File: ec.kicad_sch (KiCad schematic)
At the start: 50 parts, among them IC1 ADM3260ARSZ-RL7, J1 EC, J2 Temp, U2 ADS1115IDGS, U4 TPS60400DBV, U5 LM324, U6 MCP4017T-502E/LT

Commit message: Update files to KiCad 10.0
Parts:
- U2: footprint Package_SO:VSSOP-10_3x3mm_P0.5mm -> Package_SO:TSSOP-10_3x3mm_P0.5mm

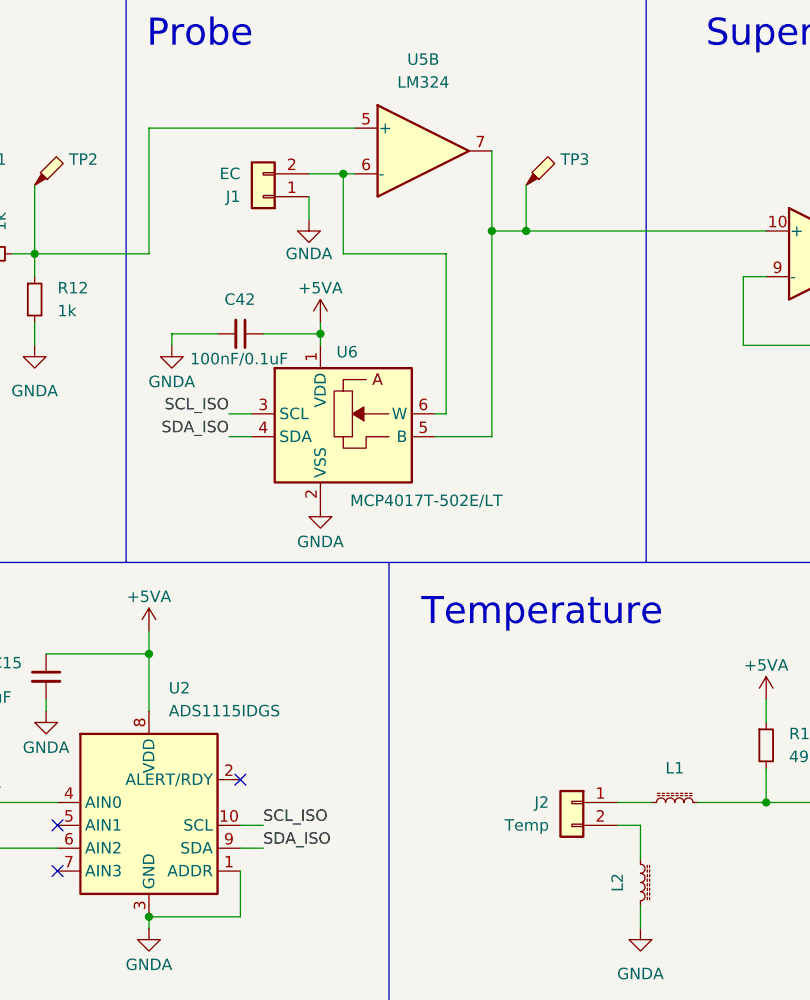
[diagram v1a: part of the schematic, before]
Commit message: Update fabrication properties
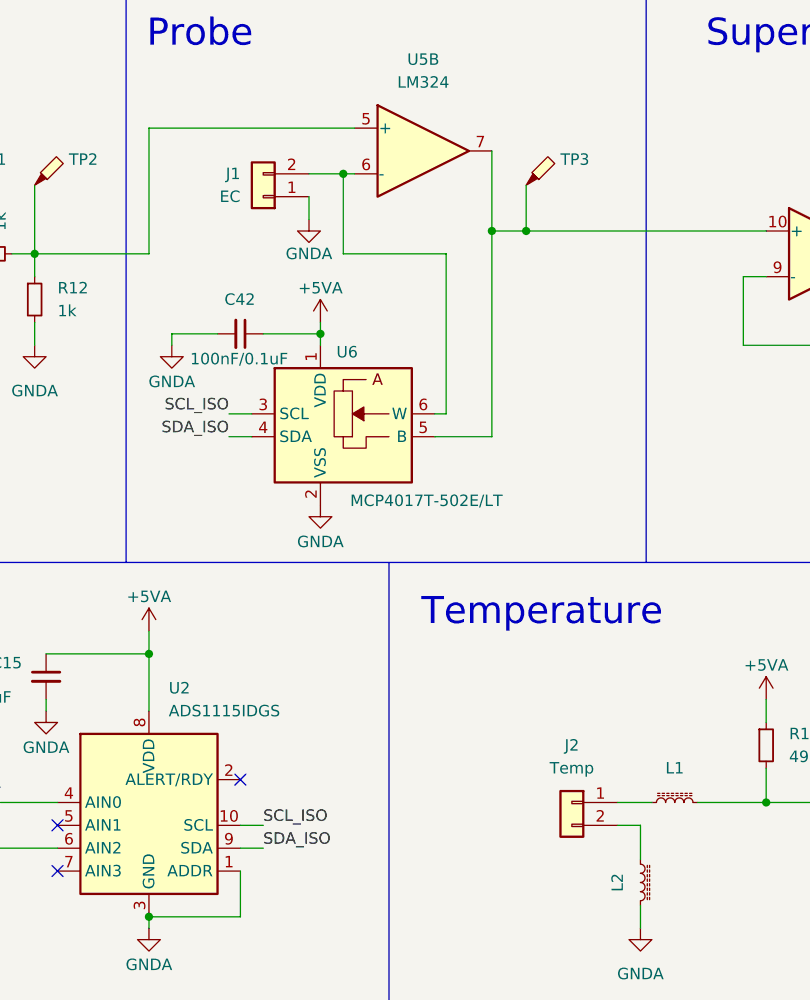
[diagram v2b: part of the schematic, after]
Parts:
- J1: value EC -> S2B-XH-A(LF)(SN)
- J2: value Temp -> S2B-XH-A(LF)(SN)
- R1: LCSC C23022 -> C2930090
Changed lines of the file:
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@@
 		(in_bom no)
 		(on_board yes)
-		(in_pos_files yes)
+		(in_pos_files no)
 		(dnp no)
 		(fields_autoplaced yes)
@@
 		(in_bom no)
 		(on_board yes)
-		(in_pos_files yes)
+		(in_pos_files no)
 		(dnp no)
 		(fields_autoplaced yes)
@@
 		(in_bom no)
 		(on_board yes)
-		(in_pos_files yes)
+		(in_pos_files no)
 		(dnp no)
 		(property "Reference" "TP5"
@@
 		(in_pos_files yes)
 		(dnp no)
+		(fields_autoplaced yes)
 		(property "Reference" "J1"
-			(at 161.29 35.5601 0)
+			(at 161.29 33.0199 0)
 			(show_name no)
 			(do_not_autoplace no)
@@
 			)
 		)
-		(property "Value" "EC"
+		(property "Value" "S2B-XH-A(LF)(SN)"
 			(at 161.29 33.0201 0)
+			(hide yes)
 			(show_name no)
 			(do_not_autoplace no)
@@
 			)
 		)
-		(property "Description" "Generic connector, single row, 01x02, script generated (kicad-library-utils/schlib/autogen/connector/)"
-			(at 163.83 35.56 0)
-			(hide yes)
+		(property "Description" "EC"
+			(at 161.29 35.5599 0)
 			(show_name no)
 			(do_not_autoplace no)
@@
 					(size 1.27 1.27)
 				)
+				(justify left)
 			)
 		)
@@
 			)
 		)
-		(property "LCSC alt" ""
-			(at 163.83 35.56 0)
-			(hide yes)
-			(show_name no)
-			(do_not_autoplace no)
-			(effects
-				(font
-					(size 1.27 1.27)
-				)
-			)
-		)
 		(property "JLCPCB Position Offset" "0,3.5"
 			(at 163.83 35.56 0)
@@
 		(in_bom no)
 		(on_board yes)
-		(in_pos_files yes)
+		(in_pos_files no)
 		(dnp no)
 		(fields_autoplaced yes)
@@
 		(in_bom no)
 		(on_board yes)
-		(in_pos_files yes)
+		(in_pos_files no)
 		(dnp no)
 		(fields_autoplaced yes)
@@
 			)
 		)
-		(property "LCSC" "C23022"
-			(at 90.17 120.65 0)
-			(hide yes)
-			(show_name no)
-			(do_not_autoplace no)
-			(effects
-				(font
-					(size 1.27 1.27)
-				)
-			)
-		)
-		(property "LCSC alt" ""
+		(property "LCSC" "C2930090"
 			(at 90.17 120.65 0)
 			(hide yes)
@@
 		(in_pos_files yes)
 		(dnp no)
+		(fields_autoplaced yes)
 		(property "Reference" "J2"
-			(at 195.58 102.8699 0)
+			(at 198.12 96.52 0)
 			(show_name no)
 			(do_not_autoplace no)
@@
 					(size 1.27 1.27)
 				)
-				(justify left)
 			)
 		)
-		(property "Value" "Temp"
+		(property "Value" "S2B-XH-A(LF)(SN)"
 			(at 195.58 105.4099 0)
+			(hide yes)
 			(show_name no)
 			(do_not_autoplace no)
@@
 			)
 		)
-		(property "Description" "Generic connector, single row, 01x02, script generated (kicad-library-utils/schlib/autogen/connector/)"
-			(at 198.12 102.87 0)
-			(hide yes)
+		(property "Description" "Temp"
+			(at 198.12 99.06 0)
 			(show_name no)
 			(do_not_autoplace no)

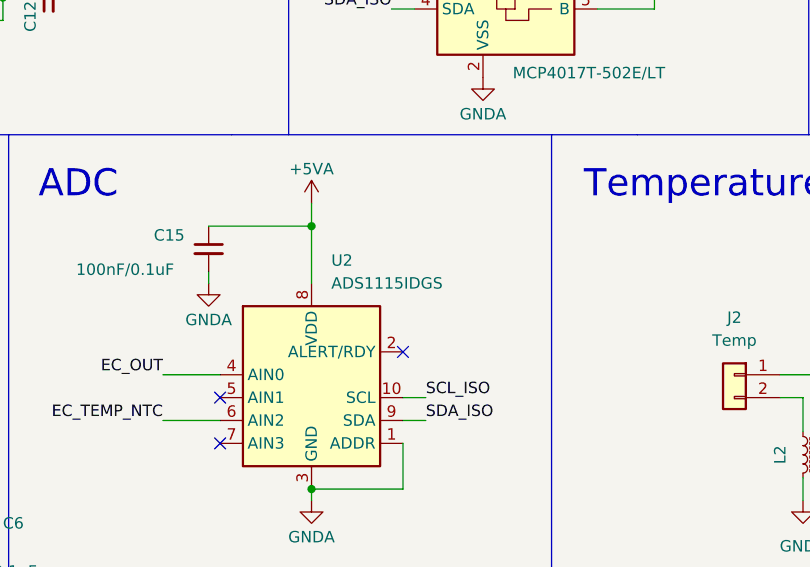
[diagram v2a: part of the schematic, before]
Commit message: Change package if ADS1115 ADC Smaller, in stock and cheaper
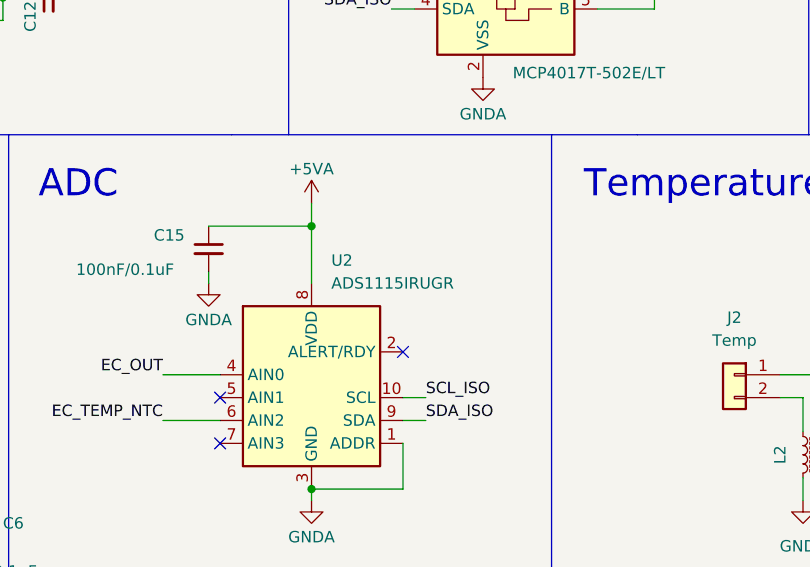
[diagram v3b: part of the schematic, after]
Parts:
- C15: footprint Capacitor_SMD:C_0603_1608Metric -> Capacitor_SMD:C_0402_1005Metric; LCSC C14663 -> C1525
- U2: value ADS1115IDGS -> ADS1115IRUGR; footprint Package_SO:TSSOP-10_3x3mm_P0.5mm -> Package_DFN_QFN:Texas_UQFN-10_1.5x2mm_P0.5mm; LCSC C37593 -> C2651328
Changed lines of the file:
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@@
 			)
 		)
-		(property "Value" "ADS1115IDGS"
+		(property "Value" "ADS1115IRUGR"
 			(at 153.3241 92.71 0)
 			(show_name no)
@@
 			)
 		)
-		(property "Footprint" "Package_SO:TSSOP-10_3x3mm_P0.5mm"
+		(property "Footprint" "Package_DFN_QFN:Texas_UQFN-10_1.5x2mm_P0.5mm"
 			(at 151.13 118.11 0)
 			(hide yes)
@@
 			)
 		)
-		(property "LCSC" "C37593"
+		(property "LCSC" "C2651328"
 			(at 151.13 105.41 0)
 			(hide yes)
@@
 			)
 		)
-		(property "Footprint" "Capacitor_SMD:C_0603_1608Metric"
+		(property "Footprint" "Capacitor_SMD:C_0402_1005Metric"
 			(at 139.7 88.9 0)
 			(hide yes)
@@
 			)
 		)
-		(property "LCSC" "C14663"
+		(property "LCSC" "C1525"
 			(at 139.7 88.9 0)
 			(hide yes)

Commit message: Update fabrication properties
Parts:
- IC1, U2: FT Rotation Offset (none) -> 270; JLCPCB Rotation Offset 270 -> (none)
- J1, J2: FT Rotation Offset (none) -> 180; JLCPCB Position Offset 0,3.5 -> (none); JLCPCB Rotation Offset 180 -> (none)
- U6: FT Rotation Offset (none) -> 90; JLCPCB Rotation Offset 90 -> (none)
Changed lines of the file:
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@@
 			)
 		)
-		(property "JLCPCB Rotation Offset" "270"
+		(property "FT Rotation Offset" "270"
 			(at 151.13 105.41 0)
 			(hide yes)
@@
 			)
 		)
-		(property "JLCPCB Position Offset" "0,3.5"
-			(at 163.83 35.56 0)
-			(hide yes)
-			(show_name no)
-			(do_not_autoplace no)
-			(effects
-				(font
-					(size 1.27 1.27)
-				)
-			)
-		)
-		(property "JLCPCB Rotation Offset" "180"
+		(property "FT Rotation Offset" "180"
 			(at 163.83 35.56 0)
 			(hide yes)
@@
 			)
 		)
-		(property "JLCPCB Rotation Offset" "270"
+		(property "FT Rotation Offset" "270"
 			(at 40.64 107.95 0)
 			(hide yes)
@@
 			)
 		)
-		(property "JLCPCB Rotation Offset" "180"
-			(at 198.12 102.87 0)
-			(hide yes)
-			(show_name no)
-			(do_not_autoplace no)
-			(effects
-				(font
-					(size 1.27 1.27)
-				)
-			)
-		)
-		(property "JLCPCB Position Offset" "0,3.5"
+		(property "FT Rotation Offset" "180"
 			(at 198.12 102.87 0)
 			(hide yes)
@@
 			)
 		)
-		(property "JLCPCB Rotation Offset" "90"
+		(property "FT Rotation Offset" "90"
 			(at 172.72 62.23 0)
 			(hide yes)
